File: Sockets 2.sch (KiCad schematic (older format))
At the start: 0 parts

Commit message: Improve schematics add new elements
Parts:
- added 1nF, 1nF?: C, symbol Device:C
- added D? (x2): 1N4448WS-7-F, Diode_SMD:D_SOD-323, symbol Device:D_ALT
- added F? (x2): SN010-60, Fuse:Fuse_1206_3216Metric, symbol Device:Polyfuse
- added J?: TABLE SENSOR, Connector_JST:JST_PH_B2B-PH-K_1x03_P2.00mm_Vertical, symbol Connector:Conn_01x03_Male
- added J?: PHOTO SENSOR RECEIVER, Connector_JST:JST_PH_B2B-PH-K_1x03_P2.00mm_Vertical, symbol Connector:Conn_01x03_Male
- added J?: PHOTO SENSOR EMITER, Connector_JST:JST_PH_B2B-PH-K_1x02_P2.00mm_Vertical, symbol Connector:Conn_01x02_Male
- added Q? (x2): BC817, Package_TO_SOT_SMD:SOT-23, symbol Transistor_BJT:BC817
- added R? (x4): 10kΩ, Resistor_SMD:R_0603_1608Metric, symbol Device:R
- added R? (x2): 33kΩ, Resistor_SMD:R_0603_1608Metric, symbol Device:R
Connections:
- new net: F?.2, J?.1 (Pin_1), R?.1
- new net: J?.2 (Pin_2), R?.2, R?.2 (x2)
- new net: D?.1 (K), Q?.1 (B), R?.1 (x2)
- new net: F?.2, J?.1 (Pin_1), J?.1 (Pin_1), R?.1
- new net +3V3: R?.1, R?.1
- new net GND: 1nF.2, 1nF?.2, D?.2 (A), D?.2 (A), J?.2 (Pin_2), J?.3 (Pin_3), J?.3 (Pin_3), Q?.2 (E), Q?.2 (E)
- new net PHOTO_SENSOR: 1nF?.1, Q?.3 (C), R?.2
- new net TABLE_SENSOR: 1nF.1, Q?.3 (C), R?.2
- new net VS: F?.1, F?.1
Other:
- note added: "NPN NC"
- note removed: "Gniazdo USB B\nSWD\nUART"

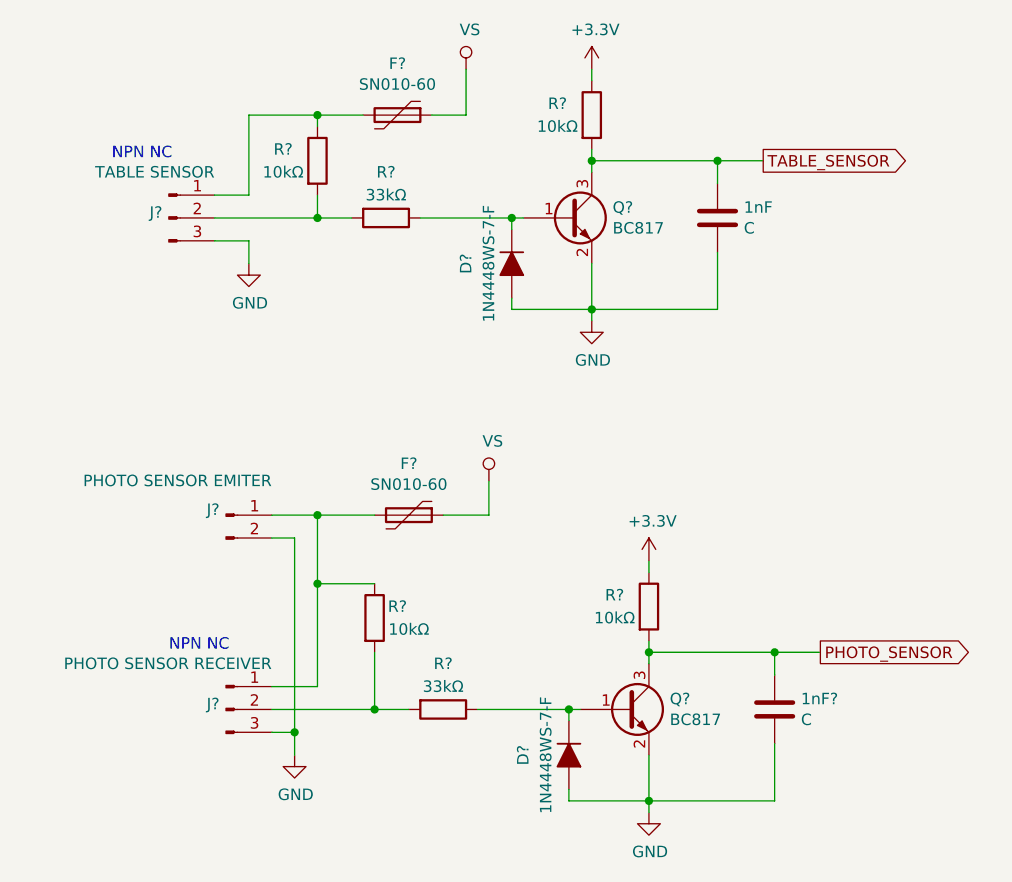
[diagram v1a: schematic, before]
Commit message: Numbering and finishing the schematic
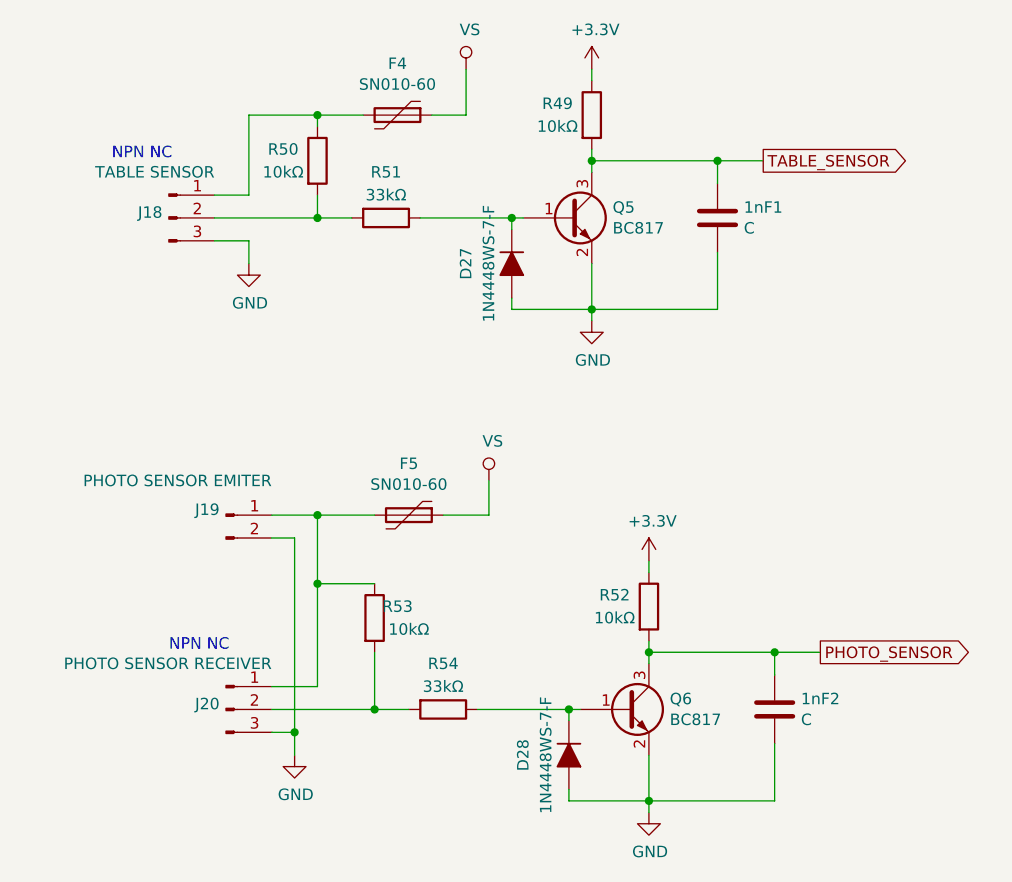
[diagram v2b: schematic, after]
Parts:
- gave numbers to parts that had none: 16
- renumbered 1nF to 1nF1
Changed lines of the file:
@@
 P 1150 1700
 AR Path="/5E07245F/5E173A89" Ref="J?"  Part="1"
-AR Path="/5E858220/5E173A89" Ref="J?"  Part="1"
-F 0 "J?" H 1122 1724 50  0000 R CNN
+AR Path="/5E858220/5E173A89" Ref="J18"  Part="1"
+F 0 "J18" H 1122 1724 50  0000 R CNN
 F 1 "TABLE SENSOR" H 1350 1900 50  0000 R CNN
 F 2 "Connector_JST:JST_PH_B2B-PH-K_1x03_P2.00mm_Vertical" H 1150 1700 50  0001 C CNN
@@
 P 2450 1050
 AR Path="/5E07245F/5E173AD0" Ref="#PWR?"  Part="1"
-AR Path="/5E858220/5E173AD0" Ref="#PWR?"  Part="1"
-F 0 "#PWR?" H 2250 900 50  0001 C CNN
+AR Path="/5E858220/5E173AD0" Ref="#PWR0131"  Part="1"
+F 0 "#PWR0131" H 2250 900 50  0001 C CNN
 F 1 "VS" H 2467 1223 50  0000 C CNN
 F 2 "" H 2450 1050 50  0001 C CNN
@@
 P 2150 1250
 AR Path="/5E07245F/5E173ADD" Ref="F?"  Part="1"
-AR Path="/5E858220/5E173ADD" Ref="F?"  Part="1"
-F 0 "F?" V 1925 1250 50  0000 C CNN
+AR Path="/5E858220/5E173ADD" Ref="F4"  Part="1"
+F 0 "F4" V 1925 1250 50  0000 C CNN
 F 1 "SN010-60 " V 2016 1250 50  0000 C CNN
 F 2 "Fuse:Fuse_1206_3216Metric" H 2200 1050 50  0001 L CNN
@@
 P 1500 1900
 AR Path="/5E07245F/5E17A8E3" Ref="#PWR?"  Part="1"
-AR Path="/5E858220/5E17A8E3" Ref="#PWR?"  Part="1"
-F 0 "#PWR?" H 1500 1650 50  0001 C CNN
+AR Path="/5E858220/5E17A8E3" Ref="#PWR0133"  Part="1"
+F 0 "#PWR0133" H 1500 1650 50  0001 C CNN
 F 1 "GND" H 1505 1727 50  0000 C CNN
 F 2 "" H 1500 1900 50  0001 C CNN
@@
 P 1800 1450
 AR Path="/5E07245F/5E17BAB2" Ref="R?"  Part="1"
-AR Path="/5E858220/5E17BAB2" Ref="R?"  Part="1"
-F 0 "R?" H 1650 1500 50  0000 C CNN
+AR Path="/5E858220/5E17BAB2" Ref="R50"  Part="1"
+F 0 "R50" H 1650 1500 50  0000 C CNN
 F 1 "10kΩ" H 1650 1400 50  0000 C CNN
 F 2 "Resistor_SMD:R_0603_1608Metric" V 1730 1450 50  0001 C CNN
@@
 	1800 1700 1800 1600
 $Comp
-L Transistor_BJT:BC817 Q?
+L Transistor_BJT:BC817 Q5
 U 1 1 5E17E162
 P 2900 1700
-F 0 "Q?" H 3091 1746 50  0000 L CNN
+F 0 "Q5" H 3091 1746 50  0000 L CNN
 F 1 "BC817" H 3091 1655 50  0000 L CNN
 F 2 "Package_TO_SOT_SMD:SOT-23" H 3100 1625 50  0001 L CIN
@@
 P 2100 1700
 AR Path="/5E07245F/5E17F7E4" Ref="R?"  Part="1"
-AR Path="/5E858220/5E17F7E4" Ref="R?"  Part="1"
-F 0 "R?" V 1900 1700 50  0000 C CNN
+AR Path="/5E858220/5E17F7E4" Ref="R51"  Part="1"
+F 0 "R51" V 1900 1700 50  0000 C CNN
 F 1 "33kΩ" V 2000 1700 50  0000 C CNN
 F 2 "Resistor_SMD:R_0603_1608Metric" V 2030 1700 50  0001 C CNN
@@
 AR Path="/5E1018C2/5E182EF0" Ref="D?"  Part="1"
 AR Path="/5E91D7CC/5E182EF0" Ref="D?"  Part="1"
-AR Path="/5E858220/5E182EF0" Ref="D?"  Part="1"
-F 0 "D?" H 2650 1700 50  0000 C CNN
+AR Path="/5E858220/5E182EF0" Ref="D27"  Part="1"
+F 0 "D27" H 2650 1700 50  0000 C CNN
 F 1 "1N4448WS-7-F" H 2650 1800 50  0000 C CNN
 F 2 "Diode_SMD:D_SOD-323" H 2650 1900 50  0001 C CNN
@@
 P 3000 2150
 AR Path="/5E07245F/5E18427F" Ref="#PWR?"  Part="1"
-AR Path="/5E858220/5E18427F" Ref="#PWR?"  Part="1"
-F 0 "#PWR?" H 3000 1900 50  0001 C CNN
+AR Path="/5E858220/5E18427F" Ref="#PWR0134"  Part="1"
+F 0 "#PWR0134" H 3000 1900 50  0001 C CNN
 F 1 "GND" H 3005 1977 50  0000 C CNN
 F 2 "" H 3000 2150 50  0001 C CNN
@@
 P 3000 1250
 AR Path="/5E07245F/5E185B5B" Ref="R?"  Part="1"
-AR Path="/5E858220/5E185B5B" Ref="R?"  Part="1"
-F 0 "R?" H 2850 1300 50  0000 C CNN
+AR Path="/5E858220/5E185B5B" Ref="R49"  Part="1"
+F 0 "R49" H 2850 1300 50  0000 C CNN
 F 1 "10kΩ" H 2850 1200 50  0000 C CNN
 F 2 "Resistor_SMD:R_0603_1608Metric" V 2930 1250 50  0001 C CNN
@@
 $EndComp
 $Comp
-L power:+3.3V #PWR?
+L power:+3.3V #PWR0132
 U 1 1 5E187914
 P 3000 1050
-F 0 "#PWR?" H 3000 900 50  0001 C CNN
+F 0 "#PWR0132" H 3000 900 50  0001 C CNN
 F 1 "+3.3V" H 3015 1223 50  0000 C CNN
 F 2 "" H 3000 1050 50  0001 C CNN
@@
 NPN NC
 $Comp
-L Device:C 1nF
+L Device:C 1nF1
 U 1 1 5E189FA4
 P 3550 1700
-F 0 "1nF" H 3665 1746 50  0000 L CNN
+F 0 "1nF1" H 3665 1746 50  0000 L CNN
 F 1 "C" H 3665 1655 50  0000 L CNN
 F 2 "" H 3588 1550 50  0001 C CNN
@@
 P 1400 3850
 AR Path="/5E07245F/5E1B90EC" Ref="J?"  Part="1"
-AR Path="/5E858220/5E1B90EC" Ref="J?"  Part="1"
-F 0 "J?" H 1372 3874 50  0000 R CNN
+AR Path="/5E858220/5E1B90EC" Ref="J20"  Part="1"
+F 0 "J20" H 1372 3874 50  0000 R CNN
 F 1 "PHOTO SENSOR RECEIVER" H 1600 4050 50  0000 R CNN
 F 2 "Connector_JST:JST_PH_B2B-PH-K_1x03_P2.00mm_Vertical" H 1400 3850 50  0001 C CNN
@@
 P 2550 2850
 AR Path="/5E07245F/5E1B90F7" Ref="#PWR?"  Part="1"
-AR Path="/5E858220/5E1B90F7" Ref="#PWR?"  Part="1"
-F 0 "#PWR?" H 2350 2700 50  0001 C CNN
+AR Path="/5E858220/5E1B90F7" Ref="#PWR0135"  Part="1"
+F 0 "#PWR0135" H 2350 2700 50  0001 C CNN
 F 1 "VS" H 2567 3023 50  0000 C CNN
 F 2 "" H 2550 2850 50  0001 C CNN
@@
 P 2200 3000
 AR Path="/5E07245F/5E1B9101" Ref="F?"  Part="1"
-AR Path="/5E858220/5E1B9101" Ref="F?"  Part="1"
-F 0 "F?" V 1975 3000 50  0000 C CNN
+AR Path="/5E858220/5E1B9101" Ref="F5"  Part="1"
+F 0 "F5" V 1975 3000 50  0000 C CNN
 F 1 "SN010-60 " V 2066 3000 50  0000 C CNN
 F 2 "Fuse:Fuse_1206_3216Metric" H 2250 2800 50  0001 L CNN
@@
 P 1700 4050
 AR Path="/5E07245F/5E1B910F" Ref="#PWR?"  Part="1"
-AR Path="/5E858220/5E1B910F" Ref="#PWR?"  Part="1"
-F 0 "#PWR?" H 1700 3800 50  0001 C CNN
+AR Path="/5E858220/5E1B910F" Ref="#PWR0137"  Part="1"
+F 0 "#PWR0137" H 1700 3800 50  0001 C CNN
 F 1 "GND" H 1705 3877 50  0000 C CNN
 F 2 "" H 1700 4050 50  0001 C CNN
@@
 P 2050 3450
 AR Path="/5E07245F/5E1B911B" Ref="R?"  Part="1"
-AR Path="/5E858220/5E1B911B" Ref="R?"  Part="1"
-F 0 "R?" H 2150 3500 50  0000 C CNN
+AR Path="/5E858220/5E1B911B" Ref="R53"  Part="1"
+F 0 "R53" H 2150 3500 50  0000 C CNN
 F 1 "10kΩ" H 2200 3400 50  0000 C CNN
 F 2 "Resistor_SMD:R_0603_1608Metric" V 1980 3450 50  0001 C CNN
@@
 	2050 3850 2050 3600
 $Comp
-L Transistor_BJT:BC817 Q?
+L Transistor_BJT:BC817 Q6
 U 1 1 5E1B912B
 P 3150 3850
-F 0 "Q?" H 3341 3896 50  0000 L CNN
+F 0 "Q6" H 3341 3896 50  0000 L CNN
 F 1 "BC817" H 3341 3805 50  0000 L CNN
 F 2 "Package_TO_SOT_SMD:SOT-23" H 3350 3775 50  0001 L CIN
@@
 P 2350 3850
 AR Path="/5E07245F/5E1B9135" Ref="R?"  Part="1"
-AR Path="/5E858220/5E1B9135" Ref="R?"  Part="1"
-F 0 "R?" V 2150 3850 50  0000 C CNN
+AR Path="/5E858220/5E1B9135" Ref="R54"  Part="1"
+F 0 "R54" V 2150 3850 50  0000 C CNN
 F 1 "33kΩ" V 2250 3850 50  0000 C CNN
 F 2 "Resistor_SMD:R_0603_1608Metric" V 2280 3850 50  0001 C CNN
@@
 AR Path="/5E1018C2/5E1B9141" Ref="D?"  Part="1"
 AR Path="/5E91D7CC/5E1B9141" Ref="D?"  Part="1"
-AR Path="/5E858220/5E1B9141" Ref="D?"  Part="1"
-F 0 "D?" H 2900 3850 50  0000 C CNN
+AR Path="/5E858220/5E1B9141" Ref="D28"  Part="1"
+F 0 "D28" H 2900 3850 50  0000 C CNN
 F 1 "1N4448WS-7-F" H 2900 3950 50  0000 C CNN
 F 2 "Diode_SMD:D_SOD-323" H 2900 4050 50  0001 C CNN
@@
 P 3250 4300
 AR Path="/5E07245F/5E1B914E" Ref="#PWR?"  Part="1"
-AR Path="/5E858220/5E1B914E" Ref="#PWR?"  Part="1"
-F 0 "#PWR?" H 3250 4050 50  0001 C CNN
+AR Path="/5E858220/5E1B914E" Ref="#PWR0138"  Part="1"
+F 0 "#PWR0138" H 3250 4050 50  0001 C CNN
 F 1 "GND" H 3255 4127 50  0000 C CNN
 F 2 "" H 3250 4300 50  0001 C CNN
@@
 P 3250 3400
 AR Path="/5E07245F/5E1B915B" Ref="R?"  Part="1"
-AR Path="/5E858220/5E1B915B" Ref="R?"  Part="1"
-F 0 "R?" H 3100 3450 50  0000 C CNN
+AR Path="/5E858220/5E1B915B" Ref="R52"  Part="1"
+F 0 "R52" H 3100 3450 50  0000 C CNN
 F 1 "10kΩ" H 3100 3350 50  0000 C CNN
 F 2 "Resistor_SMD:R_0603_1608Metric" V 3180 3400 50  0001 C CNN
@@
 $EndComp
 $Comp
-L power:+3.3V #PWR?
+L power:+3.3V #PWR0136
 U 1 1 5E1B9165
 P 3250 3200
-F 0 "#PWR?" H 3250 3050 50  0001 C CNN
+F 0 "#PWR0136" H 3250 3050 50  0001 C CNN
 F 1 "+3.3V" H 3265 3373 50  0000 C CNN
 F 2 "" H 3250 3200 50  0001 C CNN
@@
 NPN NC
 $Comp
-L Device:C 1nF?
+L Device:C 1nF2
 U 1 1 5E1B9175
 P 3800 3850
-F 0 "1nF?" H 3915 3896 50  0000 L CNN
+F 0 "1nF2" H 3915 3896 50  0000 L CNN
 F 1 "C" H 3915 3805 50  0000 L CNN
 F 2 "" H 3838 3700 50  0001 C CNN
@@
 P 1400 3000
 AR Path="/5E07245F/5E1CB1C9" Ref="J?"  Part="1"
-AR Path="/5E858220/5E1CB1C9" Ref="J?"  Part="1"
-F 0 "J?" H 1372 3024 50  0000 R CNN
+AR Path="/5E858220/5E1CB1C9" Ref="J19"  Part="1"
+F 0 "J19" H 1372 3024 50  0000 R CNN
 F 1 "PHOTO SENSOR EMITER" H 1600 3150 50  0000 R CNN
 F 2 "Connector_JST:JST_PH_B2B-PH-K_1x02_P2.00mm_Vertical" H 1400 3000 50  0001 C CNN
